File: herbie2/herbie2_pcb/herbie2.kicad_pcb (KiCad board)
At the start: 2 copper layers, 146.1 x 100.3 mm, 6 parts

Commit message: updated PCB
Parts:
- removed B1: ARDUINO_UNO_R3_SHIELD_ICSP-NO_LABELS, Sparkfun_boards:UNO_R3_SHIELD_ICSP_NOLABELS
- added D1: LED, LED_SMD:LED_1206_3216Metric, F.Cu at (152.4, 44.5)
- added D2: LED, LED_SMD:LED_1206_3216Metric, F.Cu at (152.4, 47.8)
- added D3: LED, LED_SMD:LED_1206_3216Metric, F.Cu at (158.1, 44.5)
- added D4: LED, LED_SMD:LED_1206_3216Metric, F.Cu at (158.1, 47.8)
- added J1: Screw_Terminal_01x04, TerminalBlock:TerminalBlock_bornier-4_P5.08mm, F.Cu at (193.0, 47.0)
- added J2: Screw_Terminal_01x04, TerminalBlock:TerminalBlock_bornier-4_P5.08mm, F.Cu at (170.2, 47.0)
- added J3: I2C_STANDARDQWIIC, Connectors:1X04_1MM_RA, F.Cu at (174.0, 69.8)
- added J4: Servo0, Connector_PinHeader_2.54mm:PinHeader_1x03_P2.54mm_Vertical, F.Cu at (205.7, 58.4)
- added J5: Servo1, Connector_PinHeader_2.54mm:PinHeader_1x03_P2.54mm_Vertical, F.Cu at (210.4, 58.4)
- added J6: Servo2, Connector_PinHeader_2.54mm:PinHeader_1x03_P2.54mm_Vertical, F.Cu at (215.0, 58.4)
- added J7: Servo3, Connector_PinHeader_2.54mm:PinHeader_1x03_P2.54mm_Vertical, F.Cu at (219.7, 58.4)
- added J8: I2C_STANDARDQWIIC, Connectors:1X04_1MM_RA, F.Cu at (217.2, 72.4)
- added Q1: LTC4412ES6_TRMPBF, digikey-footprints:SOT-23-6, F.Cu at (207.0, 97.8)
- added Q2: LTC4412ES6_TRMPBF, digikey-footprints:SOT-23-6, F.Cu at (205.7, 81.3)
- added R1: 470K, Resistor_SMD:R_1206_3216Metric, F.Cu at (207.0, 104.1)
- added R2: 470K, Resistor_SMD:R_1206_3216Metric, F.Cu at (200.6, 80.3)
- added R3: R, Resistor_SMD:R_1206_3216Metric, F.Cu at (141.0, 44.5)
- added R4: R, Resistor_SMD:R_1206_3216Metric, F.Cu at (141.0, 47.7)
- added R5: R, Resistor_SMD:R_1206_3216Metric, F.Cu at (146.6, 44.5)
- added R6: R, Resistor_SMD:R_1206_3216Metric, F.Cu at (146.6, 47.7)
- moved H1 99.8 mm to (106.7, 44.5)
- moved H2 99.8 mm to (106.7, 132.1)
- moved H3 82.3 mm to (218.7, 132.1)
- moved H4 81.3 mm to (218.7, 44.5)
- moved B2 52.6 mm to (133.3, 86.4)
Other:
- board size 146.1 x 100.3 mm -> 124.5 x 100.3 mm

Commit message: updated PCB
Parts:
- added F1: Fuse, Fuse:Fuseholder_Blade_Mini_Keystone_3568, F.Cu at (194.3, 129.5)
- added J9: I2C_STANDARDQWIIC, Connectors:1X04_1MM_RA, F.Cu at (109.2, 54.6)
- added LCD1: LCD-16X2SILK, Displays:LCD-16X2, F.Cu at (246.4, 81.3)
- added U1: 74164, Package_SO:TSSOP-14_4.4x5mm_P0.65mm, F.Cu at (182.9, 53.3)
- added U2: 74164, Package_SO:TSSOP-14_4.4x5mm_P0.65mm, F.Cu at (192.9, 58.4)
- added U3: 74HC595, Package_SO:SOIC-16_3.9x9.9mm_P1.27mm, F.Cu at (160.0, 68.6)
- R3, R4, R5, R6: value R -> 330
- moved J4 65.3 mm to (142.2, 43.2)
- moved J5 65.3 mm to (146.9, 43.2)
- moved J6 65.3 mm to (151.5, 43.2)
- moved J7 65.3 mm to (156.2, 43.2)
- moved B2 38.1 mm to (163.8, 109.2), turned to 270 degrees
- moved R6 30.3 mm to (130.1, 73.1)
- moved D1 30.3 mm to (135.9, 69.8)
- moved D2 30.3 mm to (135.9, 73.2)
- moved D3 30.3 mm to (141.5, 69.8)
- moved D4 30.3 mm to (141.5, 73.2)
- moved R4 30.3 mm to (124.5, 73.1)
- moved R5 30.3 mm to (130.1, 69.8)
- moved R3 30.3 mm to (124.5, 69.8)
- moved J2 24.3 mm to (194.3, 44.5)
- moved J1 23.7 mm to (215.9, 53.3), turned to 270 degrees
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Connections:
- net Net-(B2-PadD10) renamed ENC1_CS
- net Net-(B2-PadD11) renamed ENC2_CS
- net Net-(B2-PadMISO) renamed ENC_MISO
- net Net-(B2-PadMOSI) renamed ENC_MOSI
- net Net-(B2-PadSCK) renamed ENC_SCK
- B2 pad 5V: Net-(B2-Pad5V) -> 5V
- B2 pad 5V_I: Net-(B2-Pad5V_I) -> 5V
- B2 pad D12: Net-(B2-PadD12) -> CLK_SERVO
- B2 pad D13: Net-(B2-PadD13) -> DATA_SERVO
- B2 pad D6: Net-(B2-PadD6) -> CLK_LCD
- B2 pad D7: Net-(B2-PadD7) -> DATA_LCD
- B2 pad GND@: Net-(B2-PadGND@) -> GND
- B2 pad GND_: Net-(B2-PadGND_) -> GND
- D1 pad 1: Net-(D1-Pad1) -> GND
- D2 pad 1: Net-(D2-Pad1) -> GND
- D3 pad 1: Net-(D3-Pad1) -> GND
- D4 pad 1: Net-(D4-Pad1) -> GND
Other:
- board size 124.5 x 100.3 mm -> 120.7 x 97.8 mm

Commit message: updated PCB and added footprint library
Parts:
- added D5: CVFD20065A, Package_TO_SOT_THT:TO-220-2_Vertical, F.Cu at (204.5, 132.1)
- added F2: Fuse, Fuse:Fuseholder_Blade_Mini_Keystone_3568, F.Cu at (205.7, 109.2)
- added J10: CONN_04JST-PTH, Connectors:JST-4-PTH, F.Cu at (108.0, 66.0)
- added J11: CONN_04JST-PTH, Connectors:JST-4-PTH, F.Cu at (215.9, 54.6)
- added Q3: Si4427, js:SO-8_3.9x4.9mm_P1.27mm_Si4427, F.Cu at (129.5, 92.7)
- added Q4: Si4427, js:SO-8_3.9x4.9mm_P1.27mm_Si4427, F.Cu at (129.5, 101.6)
- added U1: 74HC595, Package_SO:SOIC-16_3.9x9.9mm_P1.27mm, F.Cu at (157.5, 68.6)
- added U4: LS7366R, Package_SO:SOIC-14_3.9x8.7mm_P1.27mm, F.Cu at (134.6, 59.7)
- added U5: LS7366R, Package_SO:SOIC-14_3.9x8.7mm_P1.27mm, F.Cu at (147.3, 58.4)
- added U6: TCA9534, Package_SO:SOIC-16_4.55x10.3mm_P1.27mm, F.Cu at (121.9, 64.8)
- added U7: 24v13_Pololu, js:24v13_Pololu, F.Cu at (203.2, 71.1)
- B2: moved to B.Cu
- J1: value Screw_Terminal_01x04 -> GND
- J2: value Screw_Terminal_01x04 -> 5V
- Q1, Q2: value LTC4412ES6_TRMPBF -> LTC4412
- U3: value 74HC595 -> 24v13_Pololu; footprint Package_SO:SOIC-16_3.9x9.9mm_P1.27mm -> js:24v13_Pololu
- moved Q1 68.8 mm to (138.4, 102.9)
- moved Q2 68.3 mm to (138.4, 92.7)
- moved LCD1 66.3 mm to (181.6, 95.2)
- moved R1 62.3 mm to (146.1, 91.4), turned to 180 degrees
- moved R2 62.3 mm to (138.6, 86.4)
- moved U2 51.8 mm to (177.8, 108.0)
- moved U3 50.1 mm to (203.2, 94.0), turned to 90 degrees
- moved J9 48.3 mm to (109.2, 102.9)
- moved B2 33.0 mm to (132.1, 100.3), turned to 90 degrees
- moved J1 21.0 mm to (196.8, 44.5), turned to 0 degrees
- moved J2 20.3 mm to (174.0, 44.5)
- moved D3 19.3 mm to (133.9, 52.1)
- moved D4 19.3 mm to (133.9, 55.5)
- moved R4 19.3 mm to (116.8, 55.4)
- moved R6 19.3 mm to (122.5, 55.4)
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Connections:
- net Net-(B2-PadA3) renamed VIN_MEASURE
- net Net-(B2-PadA4) renamed MOT_CURRENT1
- net Net-(B2-PadA5) renamed MOT_CURRENT2
- B2 pad D10: ENC1_CS -> CLK_SERVO
- B2 pad D11: ENC2_CS -> DATA_SERVO
- B2 pad D12: CLK_SERVO -> ENC1_SS
- B2 pad D13: DATA_SERVO -> ENC2_SS
- B2 pad D2: Net-(B2-PadD2) -> LCD_E
- B2 pad D3: Net-(B2-PadD3) -> CLK_LCD
- B2 pad D4: Net-(B2-PadD4) -> DATA_LCD
- B2 pad D5: Net-(B2-PadD5) -> MOTOR1_DIR
- B2 pad D6: CLK_LCD -> MOTOR1_PWM
- B2 pad D7: DATA_LCD -> MOTOR2_DIR
- B2 pad D8: Net-(B2-PadD8) -> MOTOR2_PWM
- B2 pad D9: Net-(B2-PadD9) -> RCLK_SERVO
- B2 pad SCL: Net-(B2-PadSCL) -> SCL
- B2 pad SDA: Net-(B2-PadSDA) -> SDA
- J3 pad 2: Net-(J3-Pad2) -> 3.3V
- J3 pad 3: Net-(J3-Pad3) -> SDA
- J3 pad 4: Net-(J3-Pad4) -> SCL
- J8 pad 2: Net-(J8-Pad2) -> 3.3V
- J8 pad 3: Net-(J8-Pad3) -> SDA
- J8 pad 4: Net-(J8-Pad4) -> SCL
- J9 pad 2: Net-(J9-Pad2) -> 3.3V
- J9 pad 3: Net-(J9-Pad3) -> SDA
- J9 pad 4: Net-(J9-Pad4) -> SCL
- Q1 pad 1: Net-(Q1-Pad1) -> BATT2
- Q1 pad 3: Net-(Q1-Pad3) -> GND
- Q1 pad 6: Net-(Q1-Pad6) -> VIN_SW
- Q2 pad 1: Net-(Q2-Pad1) -> BATT1
- Q2 pad 3: Net-(Q2-Pad3) -> GND
- Q2 pad 6: Net-(Q2-Pad6) -> VIN_SW
- R1 pad 2: Net-(R1-Pad2) -> VIN_SW
- R2 pad 2: Net-(R2-Pad2) -> VIN_SW
- U1 pad 14: 5V -> 3.3V
- U1 pad 9: Net-(U1-Pad9) -> 3.3V
- U2 pad 14: 5V -> Vdd
- U2 pad 7: GND -> Vss
- U2 pad 9: Net-(U2-Pad9) -> 3.3V
- U3 pad 1: Net-(R5-Pad1) -> GND
- U3 pad 2: Net-(R4-Pad1) -> MOTOR1_DIR
- U3 pad 3: Net-(R3-Pad1) -> MOTOR1_PWM
- U3 pad 7: Net-(U3-Pad7) -> (no net)
- U3 pad 8: Net-(U3-Pad8) -> (no net)

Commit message: updated PCB
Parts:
- removed the U1 at (166.4, 52.1)
- added C1: 12pF, Capacitor_SMD:C_1206_3216Metric, F.Cu at (151.1, 85.1)
- added C2: 12pF, Capacitor_SMD:C_1206_3216Metric, F.Cu at (149.9, 74.9)
- added C3: 12pF, Capacitor_SMD:C_1206_3216Metric, F.Cu at (194.3, 53.3)
- added C4: 12pF, Capacitor_SMD:C_1206_3216Metric, F.Cu at (199.4, 53.3)
- added C5: .1uF, Capacitor_SMD:C_1206_3216Metric, F.Cu at (139.7, 71.1)
- added C6: .1uF, Capacitor_SMD:C_1206_3216Metric, F.Cu at (207.0, 54.6)
- added C7: .1uF, Capacitor_SMD:C_1206_3216Metric, F.Cu at (133.3, 64.8)
- added C8: .1uF, Capacitor_SMD:C_1206_3216Metric, F.Cu at (109.2, 86.4)
- added H10: AC_PWR, MountingHole:MountingHole_2.2mm_M2_Pad, F.Cu at (129.5, 130.8)
- added H5: GND_BATT1, MountingHole:MountingHole_2.2mm_M2_Pad, F.Cu at (156.2, 130.8)
- added H6: PWR_BATT1, MountingHole:MountingHole_2.2mm_M2_Pad, F.Cu at (147.3, 130.8)
- added H7: GND_BATT2, MountingHole:MountingHole_2.2mm_M2_Pad, F.Cu at (174.0, 130.8)
- added H8: PWR_BATT2, MountingHole:MountingHole_2.2mm_M2_Pad, F.Cu at (165.1, 130.8)
- added H9: GND_AC_PWR, MountingHole:MountingHole_2.2mm_M2_Pad, F.Cu at (138.4, 130.8)
- added J12: Vin, TerminalBlock:TerminalBlock_bornier-4_P5.08mm, F.Cu at (153.7, 44.5)
- added J13: Servo4, Connector_PinHeader_2.54mm:PinHeader_1x03_P2.54mm_Vertical, F.Cu at (130.8, 47.0)
- added J14: Servo5, Connector_PinHeader_2.54mm:PinHeader_1x03_P2.54mm_Vertical, F.Cu at (127.0, 47.0)
- added J15: Conn_01x03_Male, Connector_PinHeader_2.54mm:PinHeader_1x03_P2.54mm_Vertical, F.Cu at (186.7, 133.3)
- added J16: Conn_02x04_Odd_Even, Connector_PinHeader_2.54mm:PinHeader_2x04_P2.54mm_Vertical, F.Cu at (120.7, 41.9)
- added R10: 100, Resistor_SMD:R_1206_3216Metric, F.Cu at (205.7, 77.0)
- added R11: 100, Resistor_SMD:R_1206_3216Metric, F.Cu at (119.4, 77.5)
- added R12: 100, Resistor_SMD:R_1206_3216Metric, F.Cu at (119.4, 73.7)
- added R13: 10, Resistor_SMD:R_1206_3216Metric, F.Cu at (193.0, 83.8)
- added R14: 20K, Resistor_SMD:R_1206_3216Metric, F.Cu at (113.0, 63.5)
- added R15: 20K, Resistor_SMD:R_1206_3216Metric, F.Cu at (204.5, 85.1)
- added R16: 20K, Resistor_SMD:R_1206_3216Metric, F.Cu at (118.1, 63.5)
- added R17: 20K, Resistor_SMD:R_1206_3216Metric, F.Cu at (209.6, 85.1)
- added R18: 1M, Resistor_SMD:R_1206_3216Metric, F.Cu at (142.2, 82.5)
- added R19: 1M, Resistor_SMD:R_1206_3216Metric, F.Cu at (198.1, 63.5)
- added R7: R, Resistor_SMD:R_1206_3216Metric, F.Cu at (154.9, 61.0)
- added R8: R, Resistor_SMD:R_1206_3216Metric, F.Cu at (160.0, 61.0)
- added R9: 100, Resistor_SMD:R_1206_3216Metric, F.Cu at (205.7, 72.4)
- added U8: D36V50F5_Pololu, js:D36V50F5_Pololu, F.Cu at (177.8, 69.8)
- added Y1: 20MHz, Crystal:Crystal_SMD_5032-2Pin_5.0x3.2mm_HandSoldering, F.Cu at (146.1, 82.5)
- added Y2: 20MHz, Crystal:Crystal_SMD_5032-2Pin_5.0x3.2mm_HandSoldering, F.Cu at (196.8, 58.4)
- J4: value Servo0 -> Servo3
- J5: value Servo1 -> Servo2
- J6: value Servo2 -> Servo1
- J7: value Servo3 -> Servo0
- moved U7 93.3 mm to (121.9, 116.8), turned to 270 degrees
- moved D1 81.4 mm to (113.0, 132.1), turned to 270 degrees
- moved R3 80.0 mm to (116.8, 132.1), turned to 270 degrees
- moved D2 77.0 mm to (120.7, 132.1), turned to 90 degrees
- moved U4 73.8 mm to (208.3, 62.2)
- moved D5 67.1 mm to (141.0, 110.5), turned to 270 degrees
- moved J3 50.5 mm to (114.6, 44.3)
- moved F2 47.5 mm to (160.0, 121.9), turned to 90 degrees
- moved R6 46.5 mm to (168.9, 53.3), turned to 90 degrees
- moved R4 40.9 mm to (125.7, 95.2)
- moved D4 40.1 mm to (174.0, 53.3), turned to 90 degrees
- moved Q1 37.0 mm to (175.3, 99.1)
- moved Q3 36.9 mm to (166.4, 90.2)
- moved Q4 36.9 mm to (166.4, 99.1)
- moved F1 35.8 mm to (170.2, 121.9), turned to 90 degrees
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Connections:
- B2 pad 5V: 5V -> 5V_USB
- J1 pad 1: Net-(J1-Pad1) -> GND
- J1 pad 2: Net-(J1-Pad2) -> GND
- J1 pad 3: Net-(J1-Pad3) -> GND
- J1 pad 4: Net-(J1-Pad4) -> GND
- J2 pad 1: Net-(J2-Pad1) -> 5V
- J2 pad 2: Net-(J2-Pad2) -> 5V
- J2 pad 3: Net-(J2-Pad3) -> 5V
- J2 pad 4: Net-(J2-Pad4) -> 5V
- LCD1 pad 16: Net-(LCD1-Pad16) -> GND
- U3 pad 4: Net-(U3-Pad4) -> E_STOP1
- U4 pad 11: Net-(J11-Pad4) -> Net-(R10-Pad2)
- U4 pad 12: Net-(J11-Pad3) -> Net-(R9-Pad2)
- U5 pad 11: Net-(J10-Pad4) -> Net-(R12-Pad2)
- U5 pad 12: Net-(J10-Pad3) -> Net-(R11-Pad2)
- U6 pad 10: Net-(U6-Pad10) -> DI1
- U6 pad 11: Net-(U6-Pad11) -> DI2
- U6 pad 12: Net-(U6-Pad12) -> DI3
- U6 pad 9: Net-(U6-Pad9) -> DI0
- U7 pad 4: Net-(U7-Pad4) -> E_STOP2
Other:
- board size 120.7 x 97.8 mm -> 119.4 x 96.5 mm
- board text added: "AC+"
- board text added: "AC-"
- board text added: "B1+"
- board text added: "B1-"
- board text added: "B2+"
- board text added: "B2-"
- board text added: "Herbie v0.1"

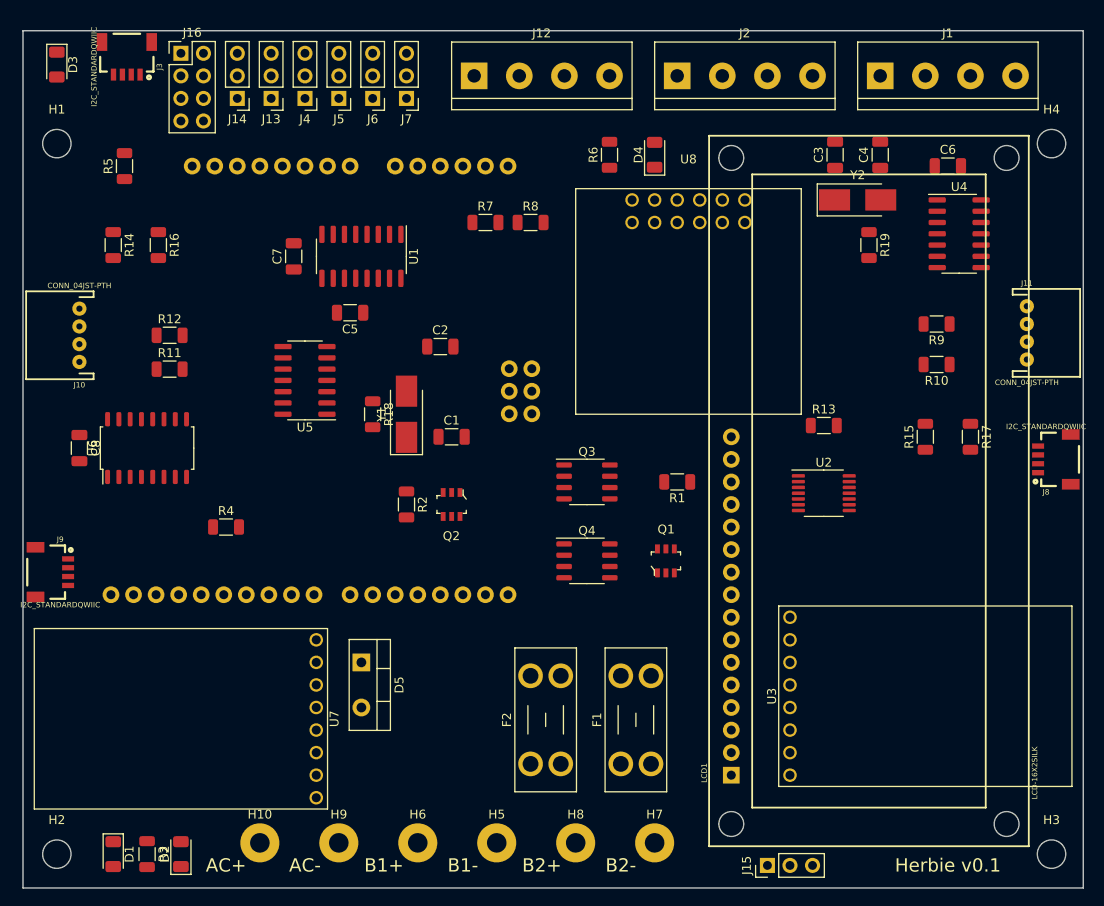
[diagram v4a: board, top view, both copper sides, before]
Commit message: started routing board
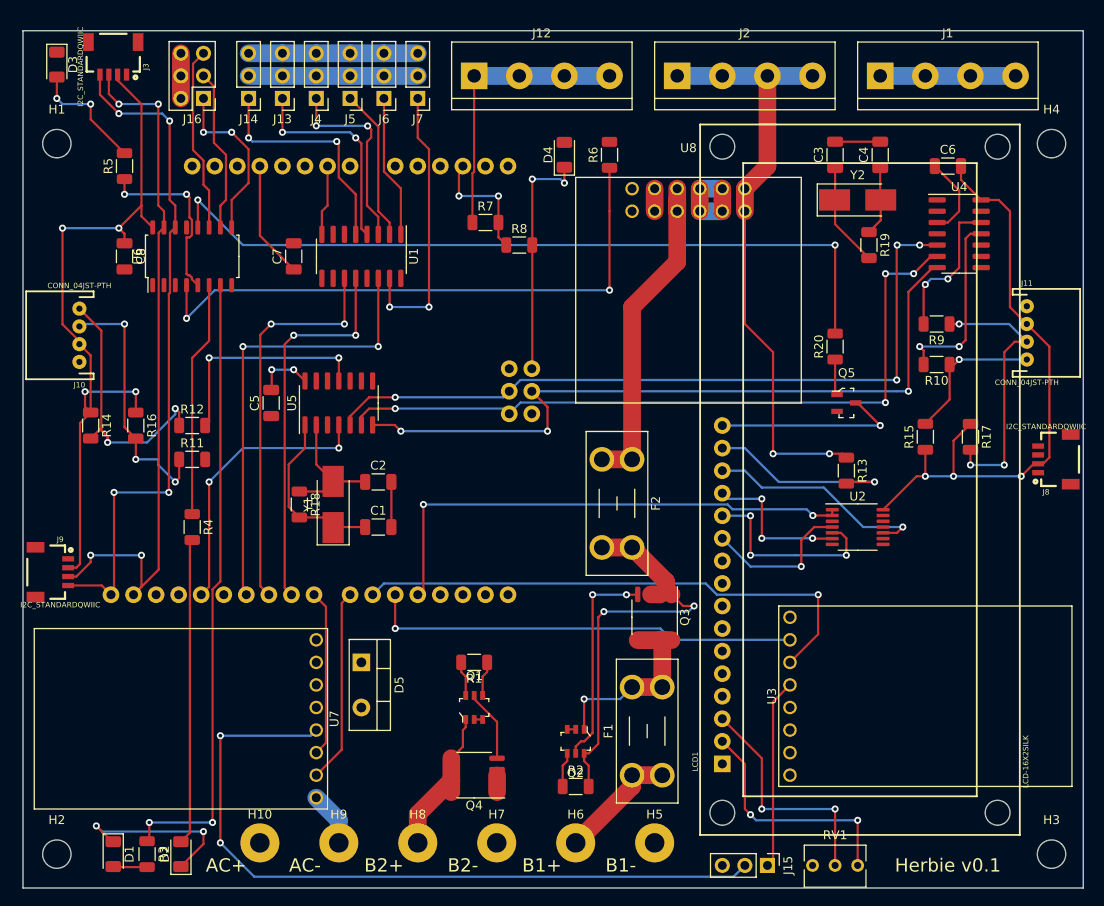
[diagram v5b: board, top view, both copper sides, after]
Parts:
- added Q5: 2N7002, digikey-footprints:SOT-23-3, F.Cu at (195.6, 81.3)
- added R20: 1K, Resistor_SMD:R_1206_3216Metric, F.Cu at (194.3, 74.9)
- added RV1: 1K, Potentiometer_THT:Potentiometer_Bourns_3266Y_Vertical, F.Cu at (196.8, 133.3)
- J16: value Conn_02x04_Odd_Even -> Conn_02x03_Odd_Even; footprint Connector_PinHeader_2.54mm:PinHeader_2x04_P2.54mm_Vertical -> Connector_PinHeader_2.54mm:PinHeader_2x03_P2.54mm_Vertical
- moved R2 37.0 mm to (165.1, 124.5), turned to 0 degrees
- moved F2 36.1 mm to (171.4, 87.6), turned to 270 degrees
- moved R1 30.6 mm to (153.7, 110.5)
- moved Q2 30.1 mm to (165.1, 119.4)
- moved Q4 27.3 mm to (153.7, 123.2), turned to 180 degrees
- moved Q1 27.2 mm to (153.7, 115.6)
- moved C8 22.2 mm to (114.3, 64.8)
- moved U6 22.2 mm to (121.9, 64.8)
- moved R14 20.5 mm to (110.5, 83.8)
- moved R16 20.5 mm to (115.6, 83.8)
- moved H5 17.8 mm to (174.0, 130.8)
- moved H6 17.8 mm to (165.1, 130.8)
- moved H7 17.8 mm to (156.2, 130.8)
- moved H8 17.8 mm to (147.3, 130.8)
- moved Q3 17.0 mm to (174.0, 105.4), turned to 270 degrees
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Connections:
- B2 pad 3.3V: Net-(B2-Pad3.3V) -> 3.3V
- D5 pad 1: VIN_SW -> VIN_FUSE
- F1 pad 1: Net-(F1-Pad1) -> BATT1
- F1 pad 2: Net-(F1-Pad2) -> BATT1_F
- F2 pad 1: Net-(F2-Pad1) -> VIN
- F2 pad 2: Net-(F2-Pad2) -> VIN_FUSE
- H10 pad 1: Net-(H10-Pad1) -> AC_PWR
- H5 pad 1: Net-(H5-Pad1) -> GND
- H6 pad 1: Net-(H6-Pad1) -> BATT1
- H7 pad 1: Net-(H7-Pad1) -> GND
- H8 pad 1: Net-(H8-Pad1) -> BATT2
- H9 pad 1: Net-(H9-Pad1) -> GND
- J12 pad 1: VIN_SW -> VIN
- J12 pad 2: VIN_SW -> VIN
- J12 pad 3: VIN_SW -> VIN
- J12 pad 4: VIN_SW -> VIN
- LCD1 pad 16: GND -> Net-(LCD1-Pad16)
- Q1 pad 6: VIN_SW -> VIN_FUSE
- Q2 pad 1: BATT1 -> BATT1_F
- Q2 pad 6: VIN_SW -> VIN_FUSE
- Q3 pad 2: VIN_SW -> VIN_FUSE
- Q3 pad 3: BATT1 -> BATT1_F
- Q4 pad 2: VIN_SW -> VIN_FUSE
- R1 pad 2: VIN_SW -> VIN_FUSE
- R2 pad 2: VIN_SW -> VIN_FUSE
- R7 pad 1: VIN_SW -> VIN
- U2 pad 14: Vdd -> 3.3V
- U2 pad 7: Vss -> GND
- U6 pad 12: DI3 -> LCD_BL
- U8 pad 3: VIN_SW -> VIN
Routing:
- net 3.3V: track 0.00 -> 171.3 mm, vias 0 -> 9
- net GND: track 0.00 -> 131.8 mm, vias 0 -> 4
- net 5V: track 0.00 -> 95.7 mm, vias 0 -> 4
- net LCD_BL: track 0.00 -> 86.9 mm, vias 0 -> 2
- net ENC_SCK: track 0.00 -> 84.6 mm, vias 0 -> 4
- net E_STOP2: track 0.00 -> 84.3 mm, vias 0 -> 2
- net ENC_MOSI: track 0.00 -> 83.2 mm, vias 0 -> 3
- net ENC_MISO: track 0.00 -> 82.5 mm, vias 0 -> 4
- net SDA: track 0.00 -> 79.7 mm, vias 0 -> 4
- net SCL: track 0.00 -> 76.8 mm, vias 0 -> 4
- net Net-(R3-Pad1): track 0.00 -> 70.2 mm, vias 0 -> 2
- net VIN: track 0.00 -> 69.1 mm
- net Net-(R6-Pad1): track 0.00 -> 66.5 mm, vias 0 -> 2
- net MOTOR1_PWM: track 0.00 -> 60.1 mm, vias 0 -> 1
- net DATA_LCD: track 0.00 -> 57.6 mm, vias 0 -> 2
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
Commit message: routed board
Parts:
- added H11: MountingHole_Pad, MountingHole:MountingHole_2.2mm_M2_Pad_TopBottom, F.Cu at (176.5, 88.9)
- added H12: MountingHole_Pad, MountingHole:MountingHole_2.2mm_M2_Pad_TopBottom, F.Cu at (106.4, 124.3)
- added H13: MountingHole_Pad, MountingHole:MountingHole_2.2mm_M2_Pad_TopBottom, F.Cu at (218.7, 106.8)
- added J17: Conn_01x03, Connector_PinHeader_2.54mm:PinHeader_1x03_P2.54mm_Vertical, F.Cu at (149.9, 50.8)
- added J18: Conn_01x02, Connector_PinHeader_2.54mm:PinHeader_1x02_P2.54mm_Vertical, F.Cu at (157.5, 97.2)
- added J19: Conn_01x01, Connector_PinHeader_2.54mm:PinHeader_1x01_P2.54mm_Vertical, F.Cu at (121.3, 51.4)
- added J20: Conn_01x03, Connector_PinHeader_2.54mm:PinHeader_1x03_P2.54mm_Vertical, F.Cu at (151.8, 76.8)
- added J4: Conn_01x01, Connector_PinHeader_2.54mm:PinHeader_1x01_P2.54mm_Vertical, F.Cu at (125.7, 51.4)
- added J5: Conn_01x02, Connector_PinHeader_2.54mm:PinHeader_1x02_P2.54mm_Vertical, F.Cu at (157.5, 50.8)
- added R21: 47K, Resistor_SMD:R_1206_3216Metric, F.Cu at (128.3, 97.2)
- added R22: 47K, Resistor_SMD:R_1206_3216Metric, F.Cu at (127.6, 81.3)
- moved J12 22.9 mm to (176.5, 44.5)
- moved J2 22.9 mm to (153.7, 44.5)
- moved Y2 1.97 mm to (198.8, 58.4)
- moved C3 1.91 mm to (196.2, 53.3)
- moved C4 1.27 mm to (200.7, 53.3)
- moved C6 1.27 mm to (205.7, 54.6)
- renumbered J7 to S0, J6 to S1, J5 to S2, J4 to S3, J13 to S4, J14 to S5
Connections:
- net 5V_USB renamed Net-(B2-Pad5V)
- B2 pad A4: MOT_CURRENT1 -> Net-(B2-PadA4)
- B2 pad A5: MOT_CURRENT2 -> Net-(B2-PadA5)
- B2 pad D10: CLK_SERVO -> MOTOR2_PWM
- B2 pad D11: DATA_SERVO -> MOTOR2_DIR
- B2 pad D5: MOTOR1_DIR -> RCLK_SERVO
- B2 pad D6: MOTOR1_PWM -> CLK_SERVO
- B2 pad D7: MOTOR2_DIR -> DATA_SERVO
- B2 pad D8: MOTOR2_PWM -> MOTOR1_DIR
- B2 pad D9: RCLK_SERVO -> MOTOR1_PWM
- J2 pad 1: 5V -> 5V_REG
- J2 pad 2: 5V -> 5V_REG
- J2 pad 3: 5V -> 5V_REG
- J2 pad 4: 5V -> 5V_REG
- LCD1 pad 2: 5V -> 5V_REG
- R13 pad 1: 5V -> 5V_REG
- RV1 pad 1: 5V -> 5V_REG
- S0 pad 2: SERVO_PWR -> 5V_REG
- S1 pad 2: SERVO_PWR -> 5V_REG
- S2 pad 2: SERVO_PWR -> 5V_REG
- S3 pad 2: SERVO_PWR -> 5V_REG
- S4 pad 2: SERVO_PWR -> 5V_REG
- S5 pad 2: SERVO_PWR -> 5V_REG
- U8 pad 1: 5V -> 5V_REG
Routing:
- net 5V_REG: track 0.00 -> 181.8 mm, vias 0 -> 6
- net 3.3V: track 171.3 -> 312.6 mm, vias 9 -> 10
- net ENC1_SS: track 0.00 -> 121.6 mm, vias 0 -> 2
- net SDA: track 79.7 -> 192.6 mm, vias 4 -> 5
- net SCL: track 76.8 -> 187.4 mm, vias 4 -> 6
- net 5V: track 95.7 -> 0.00 mm, vias 4 -> 0
- net VIN: track 69.1 -> 150.2 mm, vias 0 -> 2
- net GND: track 131.8 -> 203.0 mm, vias 4 -> 23
- net CLK_LCD: track 0.00 -> 58.7 mm, vias 0 -> 2
- net LCD_E: track 0.00 -> 50.1 mm, vias 0 -> 3
- net LCD_RS: track 0.00 -> 36.6 mm, vias 0 -> 1
- net VIN_FUSE: track 52.0 -> 83.5 mm, vias 2 -> 5
- net Net-(R11-Pad2): track 0.00 -> 29.6 mm, vias 0 -> 4
- net SERVO_PWR: track 19.0 -> 0.00 mm
- net Net-(Q2-Pad5): track 24.0 -> 38.5 mm, vias 2 -> 4
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- added copper zone on F.Cu, net 5V_REG
- added copper zone on F.Cu, net AC_PWR
- added copper zone on F.Cu, net BATT1
- added copper zone on F.Cu, net BATT1_F
- added copper zone on F.Cu, net BATT2
- added copper zone on B.Cu, net GND
- added copper zone on F.Cu, net VIN
- added copper zone on F.Cu, net VIN_FUSE
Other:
- rule via_min_size: 0.4 -> 0.7
- board text added: "+"
- board text added: "-"
- board text added: "5V"
- board text added: "E_STOP"
- board text added: "GND"
- board text added: "INT"
- board text added: "MISO"
- board text added: "MOSI"
- board text added: "RESET"
- board text added: "RX"
- board text added: "S"
- board text added: "SCK"
- board text added: "TX"
- board text added: "Vin"
